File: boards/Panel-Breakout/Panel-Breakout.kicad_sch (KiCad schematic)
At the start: 18 parts, among them J1 Raspberry_Pi_2_3, J2 BoardCon, J3 PanelLeft, J4 PanelRight, U1 ICL3232

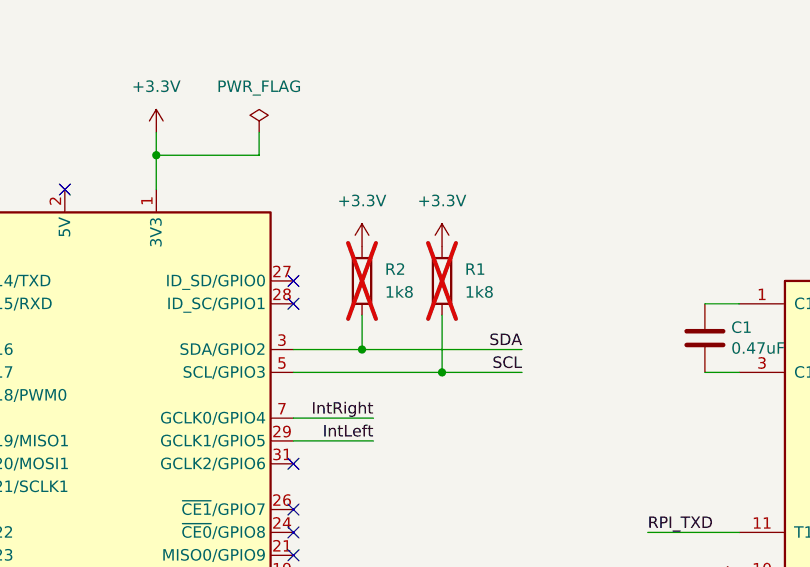
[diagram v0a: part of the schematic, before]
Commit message: Updated panel breakout board to use second I2C to avoid conflict with display
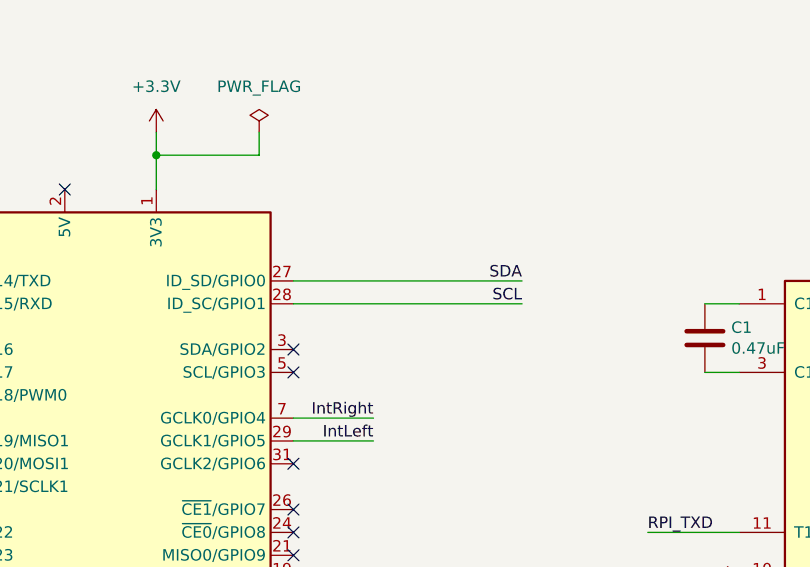
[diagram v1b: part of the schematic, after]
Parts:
- removed R1, R2: 1k8, Resistor_THT:R_Axial_DIN0207_L6.3mm_D2.5mm_P10.16mm_Horizontal, symbol Device:R
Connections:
- net SCL: now also J1.28 (ID_SC/GPIO1); no longer J1.5 (SCL/GPIO3)
- net SDA: now also J1.27 (ID_SD/GPIO0); no longer J1.3 (SDA/GPIO2)

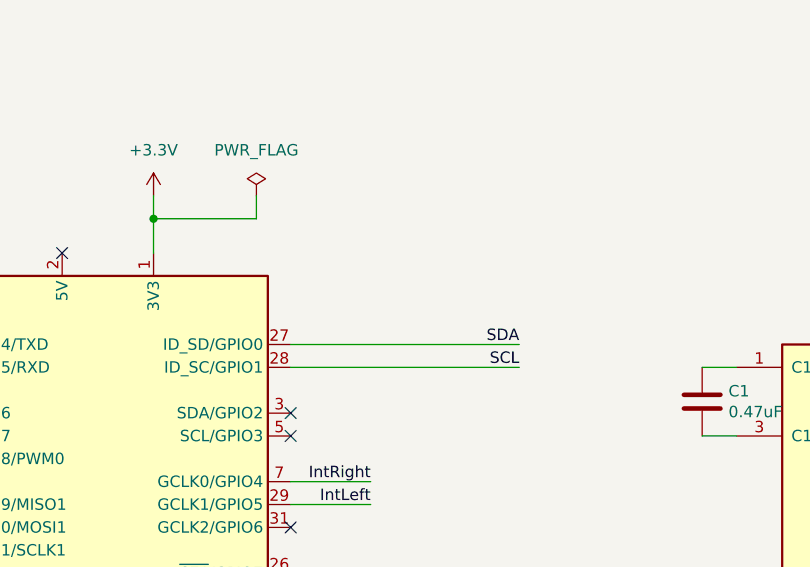
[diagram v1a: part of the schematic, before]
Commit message: Fixed missing I2C pullup for Raspberry I2C-0
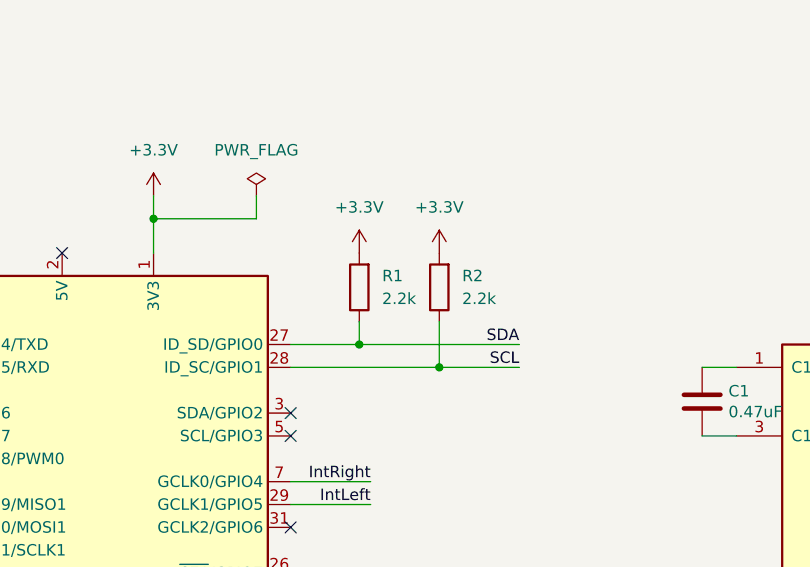
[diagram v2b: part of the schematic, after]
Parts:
- added R1, R2: 2.2k, Resistor_THT:R_Axial_DIN0207_L6.3mm_D2.5mm_P10.16mm_Horizontal, symbol Device:R
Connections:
- net +3.3V: now also R1.2, R2.2
- net SCL: now also R2.1
- net SDA: now also R1.1
